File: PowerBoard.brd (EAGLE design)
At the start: 60 x 60 mm, 84 parts, among them IC1 MCP16311, IC2 MCP16311, IC3 DS2431P, U1 BQ24090, U2 MCP1726, U3 ATTINY85V, X2 MICROMATCH-4, X3 MICROMATCH-4

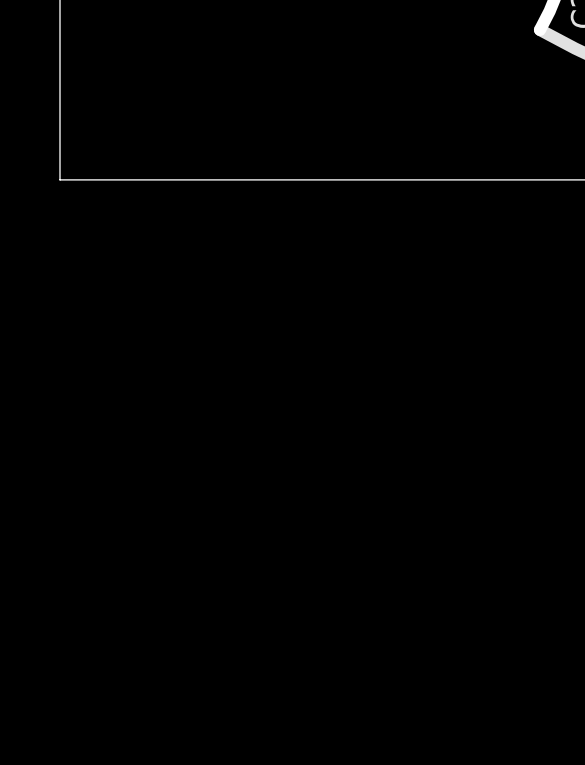
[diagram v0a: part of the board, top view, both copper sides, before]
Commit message: Added all inputs from the bringup phase of Rev0
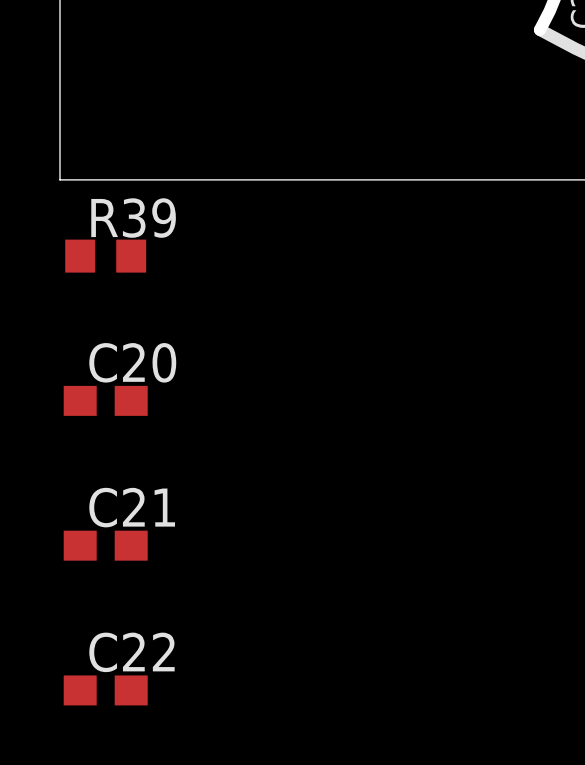
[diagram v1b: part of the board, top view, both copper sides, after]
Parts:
- added C20, C21, C22: 10n, rcl:C0603
- added R39: 20k, rcl:R0603
- C19: value 100p -> 820p
- D5, D6: value BAT54 -> BAT54*
- R17: value (none) -> 100k
- R18, R19, R20: value (none) -> 20k
- R22: value 100 -> 100*
- R23: value 0* -> 20k
- R33: value 0* -> 100
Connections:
- net GND: now also C20.1, C21.1, C22.1, R39.1
- net N$21: now also C21.2, R39.2
- net U_12: now also C22.2
- net U_BA: now also C20.2
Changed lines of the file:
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@@
 <attribute name="NAME" x="22.225" y="22.225" size="1.27" layer="25" rot="R180"/>
 </element>
-<element name="C19" library="rcl" package="C0603" value="100p" x="38.1" y="24.13" smashed="yes" rot="MR270">
+<element name="C19" library="rcl" package="C0603" value="820p" x="38.1" y="24.13" smashed="yes" rot="MR270">
 <attribute name="NAME" x="38.481" y="21.971" size="1.27" layer="26" rot="MR270"/>
 </element>
@@
 <attribute name="NAME" x="33.909" y="37.211" size="1.27" layer="25" rot="R270"/>
 </element>
-<element name="D5" library="diode" package="SOT23" value="BAT54" x="43.18" y="27.94" smashed="yes" rot="MR180">
+<element name="D5" library="diode" package="SOT23" value="BAT54*" x="43.18" y="27.94" smashed="yes" rot="MR180">
 <attribute name="NAME" x="42.037" y="31.623" size="1.27" layer="26" rot="MR180"/>
 </element>
-<element name="D6" library="diode" package="SOT23" value="BAT54" x="34.925" y="31.75" smashed="yes" rot="MR90">
+<element name="D6" library="diode" package="SOT23" value="BAT54*" x="34.925" y="31.75" smashed="yes" rot="MR90">
 <attribute name="NAME" x="35.433" y="33.782" size="1.27" layer="26" rot="MR0"/>
 </element>
@@
 <attribute name="NAME" x="40.091" y="40.951" size="1.27" layer="26" rot="MR180"/>
 </element>
-<element name="R17" library="rcl" package="R0603" value="" x="24.13" y="19.05" smashed="yes" rot="MR0">
+<element name="R17" library="rcl" package="R0603" value="100k" x="24.13" y="19.05" smashed="yes" rot="MR0">
 <attribute name="NAME" x="28.067" y="17.399" size="1.27" layer="26" rot="MR270"/>
 <attribute name="VALUE" x="24.765" y="17.145" size="1.27" layer="28" rot="MR0"/>
 </element>
-<element name="R18" library="rcl" package="R0603" value="" x="27.94" y="19.05" smashed="yes" rot="MR0">
+<element name="R18" library="rcl" package="R0603" value="20k" x="27.94" y="19.05" smashed="yes" rot="MR0">
 <attribute name="NAME" x="29.337" y="20.193" size="1.27" layer="26" rot="MR0"/>
 <attribute name="VALUE" x="28.575" y="17.145" size="1.27" layer="28" rot="MR0"/>
 </element>
-<element name="R19" library="rcl" package="R0603" value="" x="45.72" y="27.94" smashed="yes" rot="MR90">
+<element name="R19" library="rcl" package="R0603" value="20k" x="45.72" y="27.94" smashed="yes" rot="MR90">
 <attribute name="NAME" x="47.371" y="26.289" size="1.27" layer="26" rot="MR90"/>
 <attribute name="VALUE" x="43.815" y="27.305" size="1.27" layer="28" rot="MR90"/>
@@
 <attribute name="VALUE" x="24.313" y="19.01" size="1.27" layer="27" rot="R180"/>
 </element>
-<element name="R20" library="rcl" package="R0603" value="" x="44.196" y="24.13" smashed="yes" rot="MR90">
+<element name="R20" library="rcl" package="R0603" value="20k" x="44.196" y="24.13" smashed="yes" rot="MR90">
 <attribute name="NAME" x="43.561" y="18.923" size="1.27" layer="26" rot="MR90"/>
 <attribute name="VALUE" x="42.291" y="23.495" size="1.27" layer="28" rot="MR90"/>
@@
 <attribute name="NAME" x="40.005" y="29.845" size="1.27" layer="26" rot="MR90"/>
 </element>
-<element name="R22" library="rcl" package="R0603" value="100" x="40.64" y="25.4" smashed="yes" rot="MR180">
+<element name="R22" library="rcl" package="R0603" value="100*" x="40.64" y="25.4" smashed="yes" rot="MR180">
 <attribute name="NAME" x="39.243" y="21.463" size="1.27" layer="26" rot="MR180"/>
 </element>
-<element name="R23" library="rcl" package="R0603" value="0*" x="35.306" y="29.21" smashed="yes" rot="MR0">
+<element name="R23" library="rcl" package="R0603" value="20k" x="35.306" y="29.21" smashed="yes" rot="MR0">
 <attribute name="NAME" x="33.401" y="28.575" size="1.27" layer="26" rot="MR0"/>
 </element>
@@
 <attribute name="NAME" x="19.939" y="29.337" size="1.27" layer="25" rot="R270"/>
 </element>
-<element name="R33" library="rcl" package="R0603" value="0*" x="40.64" y="22.86" smashed="yes" rot="MR0">
+<element name="R33" library="rcl" package="R0603" value="100" x="40.64" y="22.86" smashed="yes" rot="MR0">
 <attribute name="NAME" x="42.291" y="18.669" size="1.27" layer="26" rot="MR0"/>
 </element>
@@
 <attribute name="NAME" x="15.621" y="28.448" size="1.27" layer="26" rot="MR0"/>
 </element>
+<element name="R39" library="rcl" package="R0603" value="20k" x="1.524" y="-2.54"/>
+<element name="C20" library="rcl" package="C0603" value="10n" x="1.524" y="-7.366"/>
+<element name="C21" library="rcl" package="C0603" value="10n" x="1.524" y="-12.192"/>
+<element name="C22" library="rcl" package="C0603" value="10n" x="1.524" y="-17.018"/>
 </elements>
 <signals>
@@
 <wire x1="6.35" y1="20.066" x2="6.816" y2="19.6" width="0.254" layer="16"/>
 <wire x1="6.816" y1="19.6" x2="9.06" y2="19.6" width="0.254" layer="16"/>
+<contactref element="R39" pad="1"/>
+<contactref element="C21" pad="1"/>
+<contactref element="C20" pad="1"/>
+<contactref element="C22" pad="1"/>
+<wire x1="0.674" y1="-2.54" x2="6.816" y2="19.6" width="0" layer="19" extent="1-16"/>
+<wire x1="0.674" y1="-7.366" x2="0.674" y2="-2.54" width="0" layer="19" extent="1-1"/>
+<wire x1="0.674" y1="-12.192" x2="0.674" y2="-7.366" width="0" layer="19" extent="1-1"/>
+<wire x1="0.674" y1="-17.018" x2="0.674" y2="-12.192" width="0" layer="19" extent="1-1"/>
 </signal>
 <signal name="N$9">
@@
 <wire x1="43.18" y1="20.32" x2="44.03" y2="19.47" width="0.4064" layer="16"/>
 <wire x1="46.355" y1="19.47" x2="44.03" y2="19.47" width="0.4064" layer="16"/>
+<contactref element="C22" pad="2"/>
+<wire x1="2.374" y1="-17.018" x2="24.98" y2="19.05" width="0" layer="19" extent="1-16"/>
 </signal>
 <signal name="U_BA">
@@
 <wire x1="43.434" y1="24.892" x2="44.362" y2="24.892" width="0.4064" layer="16"/>
 <wire x1="44.362" y1="24.892" x2="44.196" y2="24.98" width="0.4064" layer="16"/>
+<contactref element="C20" pad="2"/>
+<wire x1="2.374" y1="-7.366" x2="41.49" y2="22.86" width="0" layer="19" extent="1-16"/>
 </signal>
 <signal name="N$17">
@@
 <wire x1="36.41" y1="31.365" x2="36.156" y2="31.111" width="0.4064" layer="16"/>
 <wire x1="36.156" y1="31.111" x2="36.156" y2="29.21" width="0.4064" layer="16"/>
+<contactref element="R39" pad="2"/>
+<contactref element="C21" pad="2"/>
+<wire x1="2.374" y1="-2.54" x2="35.98" y2="26.67" width="0" layer="19" extent="1-16"/>
+<wire x1="2.374" y1="-12.192" x2="2.374" y2="-2.54" width="0" layer="19" extent="1-1"/>
 </signal>
 <signal name="AVR_RST">
